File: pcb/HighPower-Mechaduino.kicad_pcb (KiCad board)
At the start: 2 copper layers, 60 x 60 mm, 133 parts, among them J1 SUPPLY, J2 STEPPER, P1 SWD, P2 USB, P3 PoStep25-32, P4 -, P5 -, P6 -, P7 -, Q1 SSM3J328R, Q10 IPD079N06L3G, Q11 BSS138, Q2 BSS138, Q3 IPD079N06L3G, Q4 IPD079N06L3G, Q5 IPD079N06L3G, Q6 IPD079N06L3G, Q7 IPD079N06L3G, Q8 IPD079N06L3G, Q9 IPD079N06L3G, SW1 B3U-1000P, U1 AS5047D, U2 AP2112K-3.3TRG1, U3 AT24CS64-SSHM, U4 SAMD21G18A-A, U5 A4955GLPTR-T, U6 A4955GLPTR-T, U7 USBLC6-2SC6, U8 MCP16331T, U9 LM75BD, Y1 G83270022

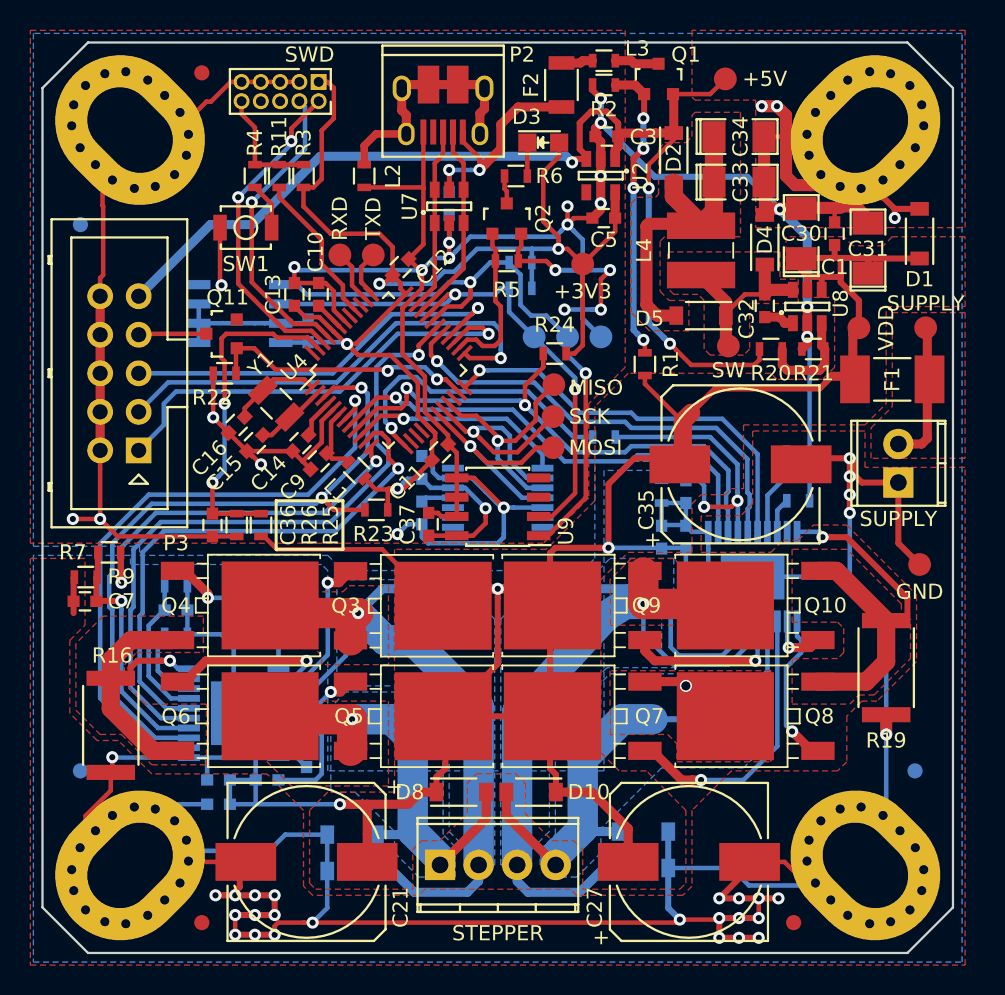
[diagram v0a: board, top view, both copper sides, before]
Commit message: Fix little schematic error
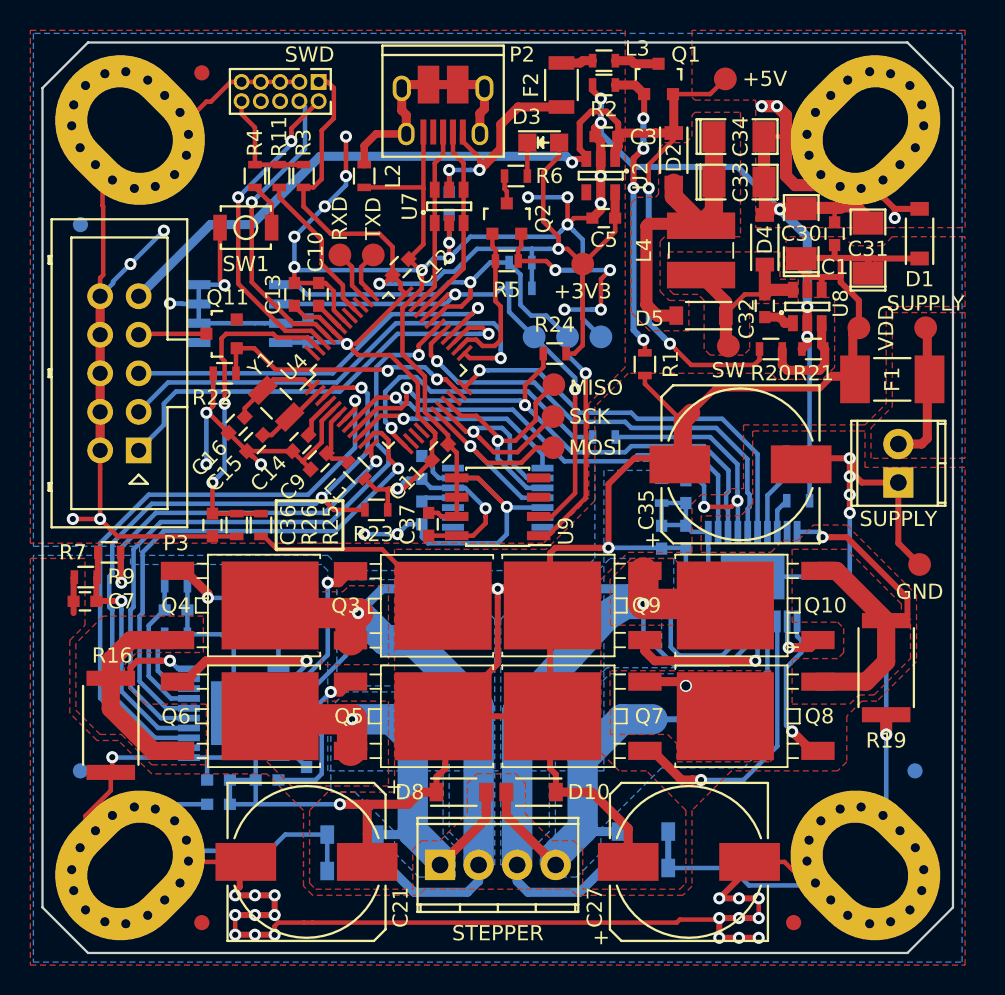
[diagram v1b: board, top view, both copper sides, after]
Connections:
- U3 pad 4: Net-(U3-Pad4) -> GND
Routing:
- net GND: track 500.4 -> 520.3 mm, vias 55 -> 61

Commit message: update mounting hole symbol
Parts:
- MK1: renamed from P4; value - -> Mounting_Hole_PAD
- MK2: renamed from P5; value - -> Mounting_Hole_PAD
- MK3: renamed from P6; value - -> Mounting_Hole_PAD
- MK4: renamed from P7; value - -> Mounting_Hole_PAD
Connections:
- P1 pad 6: Net-(P1-Pad6) -> (no net)
- P1 pad 8: Net-(P1-Pad8) -> (no net)
- P2 pad 4: /Protected_USB_Supply/ID -> (no net)
- U1 pad 10: Net-(U1-Pad10) -> (no net)
- U1 pad 14: Net-(U1-Pad14) -> (no net)
- U1 pad 6: Net-(U1-Pad6) -> (no net)
- U1 pad 7: Net-(U1-Pad7) -> (no net)
- U1 pad 8: Net-(U1-Pad8) -> (no net)
- U1 pad 9: Net-(U1-Pad9) -> (no net)
- U4 pad 14: /Arduino_Zero_Base/Arduino_D3 -> (no net)
- U4 pad 15: /Arduino_Zero_Base/Arduino_D1 -> (no net)
- U4 pad 16: /Arduino_Zero_Base/Arduino_D0 -> (no net)
- U4 pad 22: Net-(U4-Pad22) -> (no net)
- U4 pad 39: /Arduino_Zero_Base/Arduino_TX_LED -> (no net)
- U4 pad 41: /Arduino_Zero_Base/Arduino_USB_HOST_ENABLED -> (no net)
- U4 pad 48: /Arduino_Zero_Base/Arduino_RX_LED -> (no net)
- U9 pad 3: Net-(U9-Pad3) -> (no net)

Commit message: Add OSHW and KiCad logo
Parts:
- added REF***: OSHW-Logo_11.4x12mm_SilkScreen, Symbols:OSHW-Logo_11.4x12mm_SilkScreen, B.Cu at (150.0, 115.0)
- added REF***: KiCad-Logo2_8mm_SilkScreen, Symbols:KiCad-Logo2_8mm_SilkScreen, B.Cu at (168.6, 88.8)

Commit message: Improve pcb layout
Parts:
- removed W1: SUPPLY, Measurement_Points:Measurement_Point_Round-SMD-Pad_Small
- C30, C34: footprint SMD_Packages:SMD-1206_Pol -> Capacitors_SMD:c_elec_6.3x5.8
- C31, C33: value 10µ -> 100n; footprint SMD_Packages:SMD-1206_Pol -> Capacitors_SMD:C_0603
- D1: moved to B.Cu
- moved W2 20.5 mm to (157.8, 101.6)
- moved R2 16.0 mm to (157.0, 88.8), turned to 270 degrees
- moved D1 13.3 mm to (171.2, 94.2), turned to 0 degrees
- moved W3 9.07 mm to (158.2, 78.4)
- moved C30 6.62 mm to (176.0, 85.4)
- moved Q1 5.91 mm to (155.4, 75.2)
- moved D2 4.99 mm to (158.4, 73.8), turned to 90 degrees
- moved C31 3.15 mm to (171.4, 82.6)
- moved R1 2.71 mm to (157.0, 91.4)
- moved C1 2.40 mm to (169.8, 82.6)
- moved C3 2.27 mm to (155.4, 77.6)
- moved C5 2.01 mm to (155.4, 82.8)
- moved U2 1.99 mm to (155.4, 80.2)
- moved C34 1.80 mm to (164.4, 75.2)
- moved REF*** 1.80 mm to (168.6, 87.0)
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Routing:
- net GND: track 520.3 -> 538.0 mm, vias 61 -> 74
- net +3V3: track 104.5 -> 97.1 mm, vias 5 -> 6
- net VDD: track 166.7 -> 174.1 mm, vias 3 -> 5
- net Net-(C33-Pad1): track 20.7 -> 26.9 mm
- net +5V: track 74.5 -> 70.3 mm, vias 3 -> 2
- net Net-(F1-Pad2): track 9.20 -> 6.15 mm
- net Net-(Q1-Pad1): track 19.8 -> 21.9 mm, vias 4 -> 2
- net /Protected_USB_Supply/VBUS: track 2.94 -> 1.73 mm
- net Net-(D3-Pad1): track 2.20 -> 3.29 mm
- net /LED_D13: track 10.5 -> 9.63 mm
- net /OCLn2: track 37.0 -> 37.8 mm
- net /MCP16331_5V/Vfb: track 6.97 -> 6.23 mm
- net Net-(Q2-Pad3): track 1.86 -> 1.25 mm
- added copper zone on F.Cu, net +5V

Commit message: Improve pcb
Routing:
- net /PWM_Bridge_A4955-A/OUT2: track 54.8 -> 74.0 mm, vias 1 -> 16
- net /PWM_Bridge_A4955-A/OUT1: track 34.5 -> 49.6 mm, vias 1 -> 14
- net /PWM_Bridge_A4955-B/OUT1: track 59.1 -> 73.1 mm, vias 1 -> 11
- net /PWM_Bridge_A4955-B/OUT2: track 38.3 -> 52.1 mm, vias 1 -> 14
- net GND: track 538.0 -> 539.8 mm

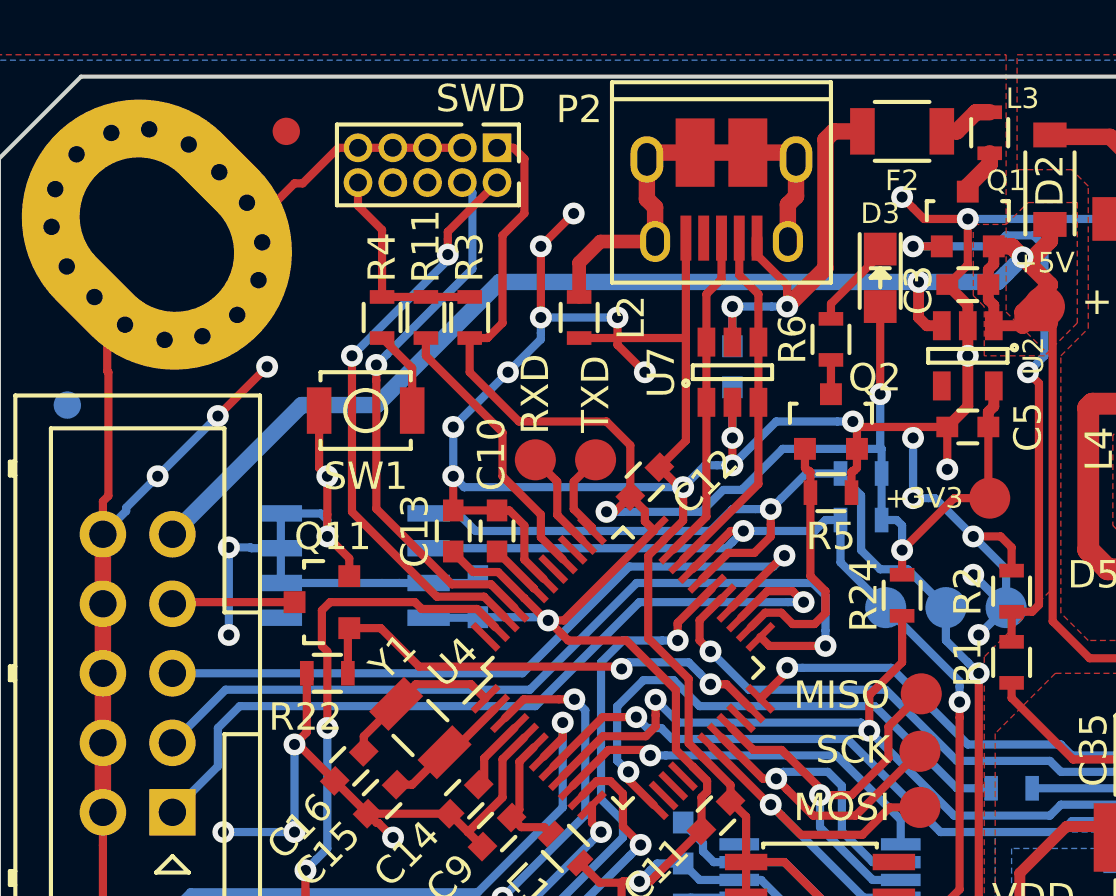
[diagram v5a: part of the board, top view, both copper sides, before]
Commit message: Add Digital IO connector
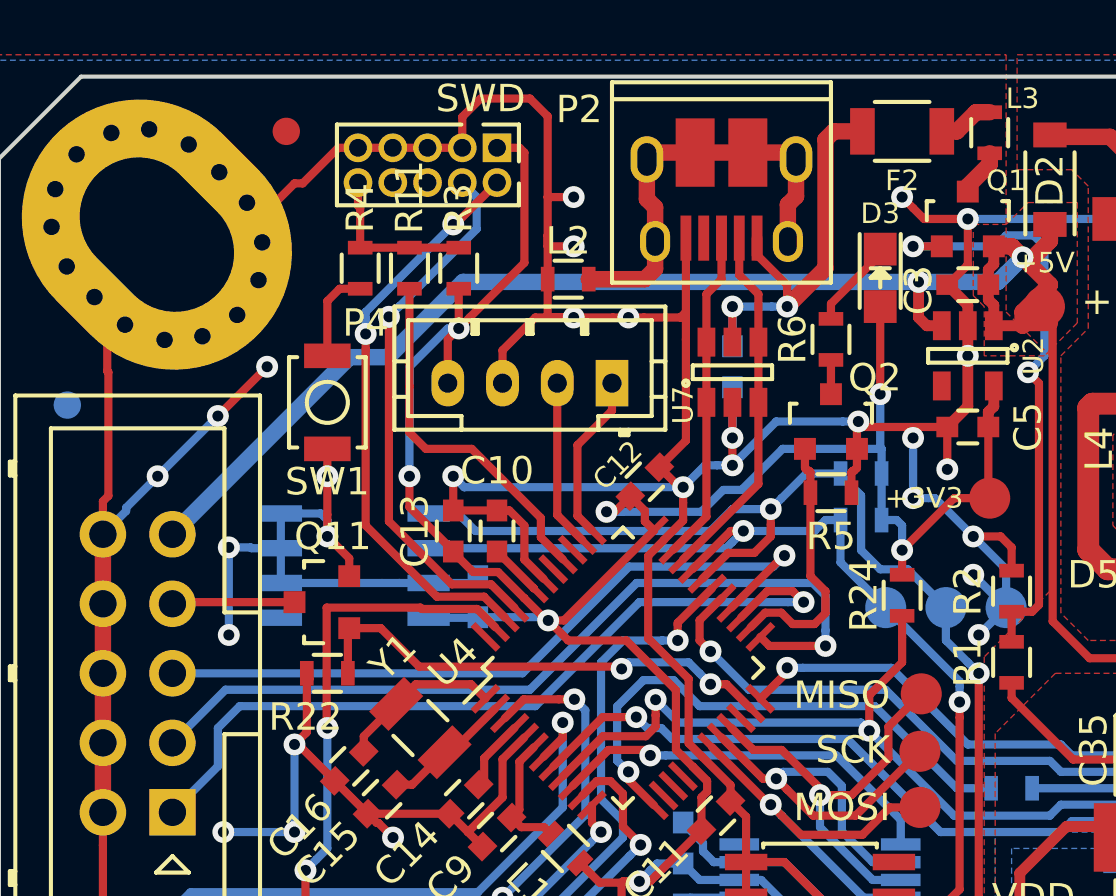
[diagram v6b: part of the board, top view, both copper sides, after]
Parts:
- removed W8: TXD, Measurement_Points:Measurement_Point_Round-SMD-Pad_Small
- removed W9: RXD, Measurement_Points:Measurement_Point_Round-SMD-Pad_Small
- added P4: CONN_01X04, Connectors_JST:JST_PH_B4B-PH-K_04x2.00mm_Straight, F.Cu at (142.4, 81.2)
- moved R4 1.97 mm to (133.2, 77.0)
- moved R11 1.90 mm to (135.0, 77.0)
- moved R3 1.84 mm to (136.8, 77.0)
- moved L2 1.46 mm to (140.8, 77.4), turned to 180 degrees
- moved SW1 1.43 mm to (132.0, 81.9), turned to 90 degrees
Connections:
- P1 pad 6: (no net) -> Net-(P1-Pad6)
- P1 pad 8: (no net) -> Net-(P1-Pad8)
- P2 pad 4: (no net) -> /Protected_USB_Supply/ID
- U1 pad 10: (no net) -> Net-(U1-Pad10)
- U1 pad 14: (no net) -> Net-(U1-Pad14)
- U1 pad 6: (no net) -> Net-(U1-Pad6)
- U1 pad 7: (no net) -> Net-(U1-Pad7)
- U1 pad 8: (no net) -> Net-(U1-Pad8)
- U1 pad 9: (no net) -> Net-(U1-Pad9)
- U4 pad 14: (no net) -> /Arduino_Zero_Base/Arduino_D3
- U4 pad 15: (no net) -> /Arduino_Zero_Base/Arduino_D1
- U4 pad 16: (no net) -> /Arduino_Zero_Base/Arduino_D0
- U4 pad 22: (no net) -> Net-(U4-Pad22)
- U4 pad 39: (no net) -> /Arduino_Zero_Base/Arduino_TX_LED
- U4 pad 41: (no net) -> /Arduino_Zero_Base/Arduino_USB_HOST_ENABLED
- U4 pad 48: (no net) -> /Arduino_Zero_Base/Arduino_RX_LED
- U9 pad 3: (no net) -> Net-(U9-Pad3)
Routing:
- net Net-(R11-Pad2): track 10.2 -> 13.2 mm
- net /Arduino_Zero_Base/Arduino_TXD: track 3.19 -> 6.12 mm
- net +3V3: track 97.1 -> 99.9 mm, vias 6 -> 8
- net /Arduino_Zero_Base/Arduino_RXD: track 3.64 -> 6.11 mm
- net /RESET: track 7.74 -> 6.01 mm
- net GND: track 539.8 -> 541.5 mm, vias 74 -> 71
- net Net-(L2-Pad1): track 17.1 -> 16.3 mm
